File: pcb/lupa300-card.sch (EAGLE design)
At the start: 41 parts

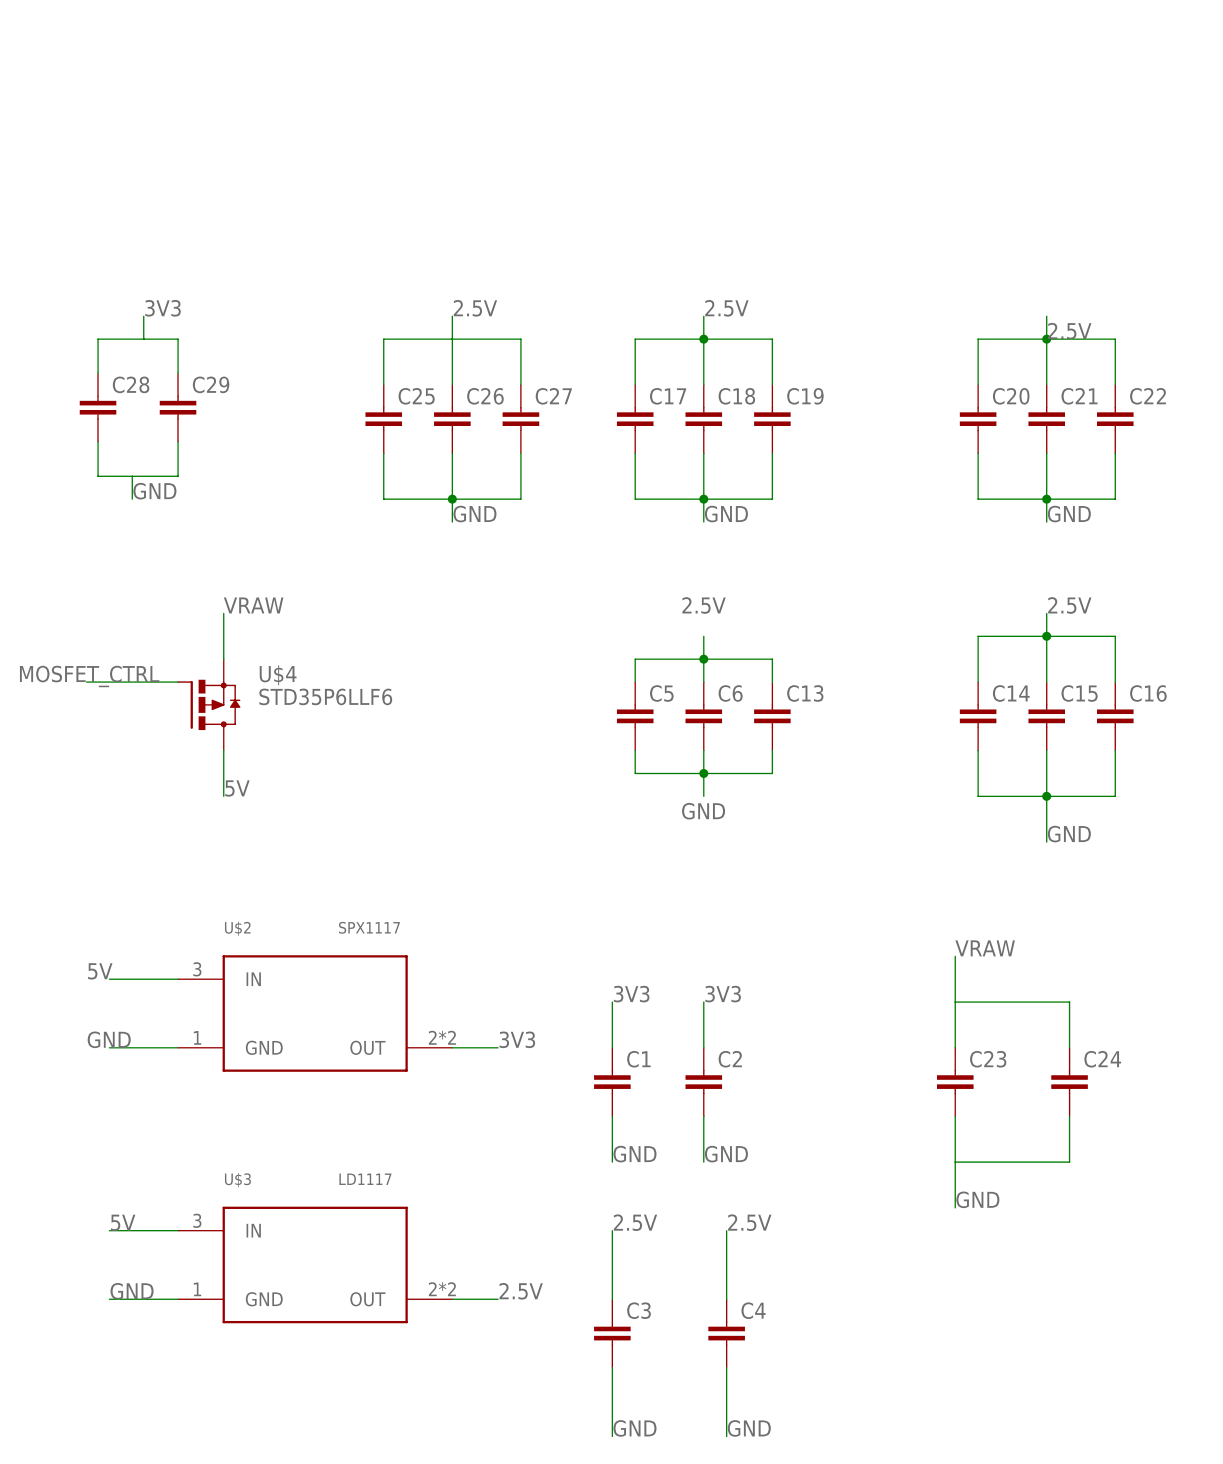
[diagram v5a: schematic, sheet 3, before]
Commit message: added all component values and added partslist
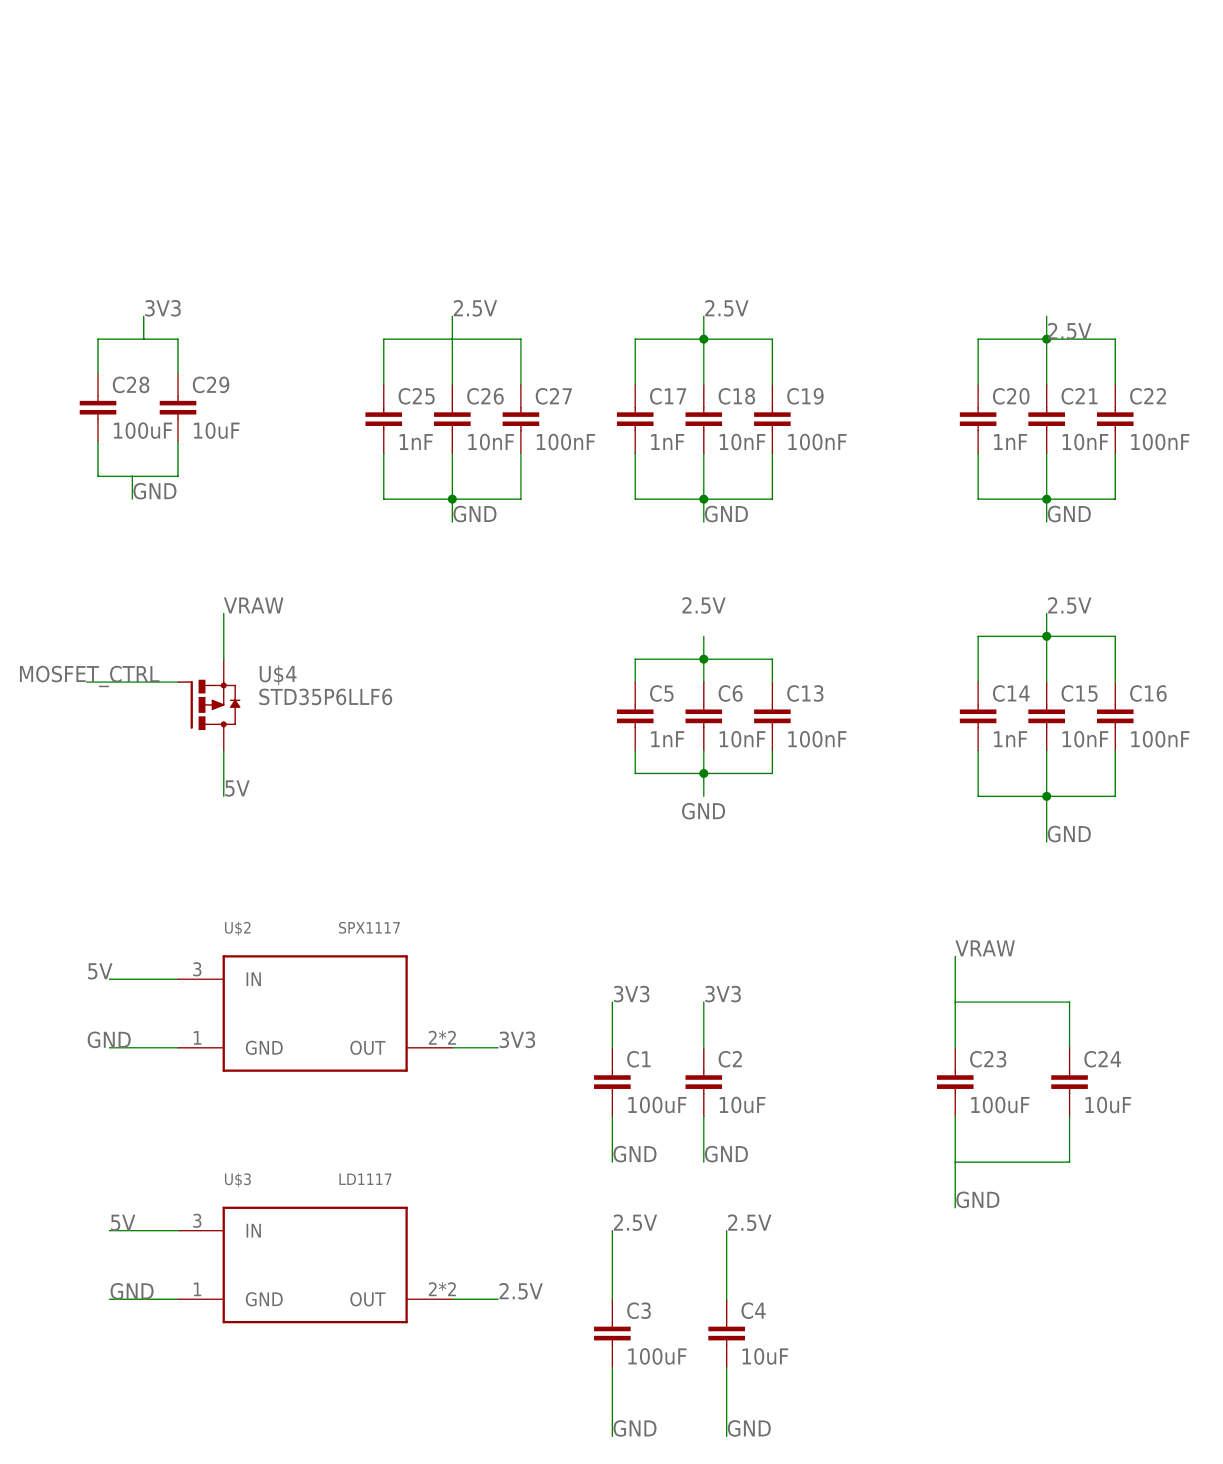
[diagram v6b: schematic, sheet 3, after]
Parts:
- C1, C23, C28, C3: value (none) -> 100uF
- C13, C16, C19, C22, C27: value (none) -> 100nF
- C14, C17, C20, C25, C5: value (none) -> 1nF
- C15, C18, C21, C26, C6: value (none) -> 10nF
- C2, C24, C29, C4: value (none) -> 10uF
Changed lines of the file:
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@@
 <?xml version="1.0" encoding="utf-8"?>
 <!DOCTYPE eagle SYSTEM "eagle.dtd">
-<eagle version="8.3.1">
+<eagle version="8.6.1">
 <drawing>
 <settings>
@@
 <part name="UZEDUPPER" library="SparkFun-Connectors" deviceset="CONN_08X2" device=""/>
 <part name="UZEDLOWER" library="SparkFun-Connectors" deviceset="CONN_08X2" device=""/>
-<part name="C1" library="rcl" library_urn="urn:adsk.eagle:library:334" deviceset="C-EU" device="C1206K" package3d_urn="urn:adsk.eagle:package:23682/2"/>
-<part name="C2" library="rcl" library_urn="urn:adsk.eagle:library:334" deviceset="C-EU" device="C1206K" package3d_urn="urn:adsk.eagle:package:23682/2"/>
-<part name="C3" library="rcl" library_urn="urn:adsk.eagle:library:334" deviceset="C-EU" device="C1206K" package3d_urn="urn:adsk.eagle:package:23682/2"/>
-<part name="C4" library="rcl" library_urn="urn:adsk.eagle:library:334" deviceset="C-EU" device="C1206K" package3d_urn="urn:adsk.eagle:package:23682/2"/>
-<part name="C5" library="rcl" library_urn="urn:adsk.eagle:library:334" deviceset="C-EU" device="C0603" package3d_urn="urn:adsk.eagle:package:23616/2"/>
-<part name="C6" library="rcl" library_urn="urn:adsk.eagle:library:334" deviceset="C-EU" device="C0603" package3d_urn="urn:adsk.eagle:package:23616/2"/>
-<part name="C13" library="rcl" library_urn="urn:adsk.eagle:library:334" deviceset="C-EU" device="C0603" package3d_urn="urn:adsk.eagle:package:23616/2"/>
-<part name="C14" library="rcl" library_urn="urn:adsk.eagle:library:334" deviceset="C-EU" device="C0603" package3d_urn="urn:adsk.eagle:package:23616/2"/>
-<part name="C15" library="rcl" library_urn="urn:adsk.eagle:library:334" deviceset="C-EU" device="C0603" package3d_urn="urn:adsk.eagle:package:23616/2"/>
-<part name="C16" library="rcl" library_urn="urn:adsk.eagle:library:334" deviceset="C-EU" device="C0603" package3d_urn="urn:adsk.eagle:package:23616/2"/>
-<part name="C17" library="rcl" library_urn="urn:adsk.eagle:library:334" deviceset="C-EU" device="C0603" package3d_urn="urn:adsk.eagle:package:23616/2"/>
-<part name="C18" library="rcl" library_urn="urn:adsk.eagle:library:334" deviceset="C-EU" device="C0603" package3d_urn="urn:adsk.eagle:package:23616/2"/>
-<part name="C19" library="rcl" library_urn="urn:adsk.eagle:library:334" deviceset="C-EU" device="C0603" package3d_urn="urn:adsk.eagle:package:23616/2"/>
-<part name="C20" library="rcl" library_urn="urn:adsk.eagle:library:334" deviceset="C-EU" device="C0603" package3d_urn="urn:adsk.eagle:package:23616/2"/>
-<part name="C21" library="rcl" library_urn="urn:adsk.eagle:library:334" deviceset="C-EU" device="C0603" package3d_urn="urn:adsk.eagle:package:23616/2"/>
-<part name="C22" library="rcl" library_urn="urn:adsk.eagle:library:334" deviceset="C-EU" device="C0603" package3d_urn="urn:adsk.eagle:package:23616/2"/>
-<part name="C23" library="rcl" library_urn="urn:adsk.eagle:library:334" deviceset="C-EU" device="C1206" package3d_urn="urn:adsk.eagle:package:23618/2"/>
-<part name="C24" library="rcl" library_urn="urn:adsk.eagle:library:334" deviceset="C-EU" device="C1206" package3d_urn="urn:adsk.eagle:package:23618/2"/>
-<part name="C25" library="rcl" library_urn="urn:adsk.eagle:library:334" deviceset="C-EU" device="C0603" package3d_urn="urn:adsk.eagle:package:23616/2"/>
-<part name="C26" library="rcl" library_urn="urn:adsk.eagle:library:334" deviceset="C-EU" device="C0603" package3d_urn="urn:adsk.eagle:package:23616/2"/>
-<part name="C27" library="rcl" library_urn="urn:adsk.eagle:library:334" deviceset="C-EU" device="C0603" package3d_urn="urn:adsk.eagle:package:23616/2"/>
-<part name="C28" library="rcl" library_urn="urn:adsk.eagle:library:334" deviceset="C-EU" device="C0603" package3d_urn="urn:adsk.eagle:package:23616/2"/>
-<part name="C29" library="rcl" library_urn="urn:adsk.eagle:library:334" deviceset="C-EU" device="C0603" package3d_urn="urn:adsk.eagle:package:23616/2"/>
+<part name="C1" library="rcl" library_urn="urn:adsk.eagle:library:334" deviceset="C-EU" device="C1206K" package3d_urn="urn:adsk.eagle:package:23682/2" value="100uF"/>
+<part name="C2" library="rcl" library_urn="urn:adsk.eagle:library:334" deviceset="C-EU" device="C1206K" package3d_urn="urn:adsk.eagle:package:23682/2" value="10uF"/>
+<part name="C3" library="rcl" library_urn="urn:adsk.eagle:library:334" deviceset="C-EU" device="C1206K" package3d_urn="urn:adsk.eagle:package:23682/2" value="100uF"/>
+<part name="C4" library="rcl" library_urn="urn:adsk.eagle:library:334" deviceset="C-EU" device="C1206K" package3d_urn="urn:adsk.eagle:package:23682/2" value="10uF"/>
+<part name="C5" library="rcl" library_urn="urn:adsk.eagle:library:334" deviceset="C-EU" device="C0603" package3d_urn="urn:adsk.eagle:package:23616/2" value="1nF"/>
+<part name="C6" library="rcl" library_urn="urn:adsk.eagle:library:334" deviceset="C-EU" device="C0603" package3d_urn="urn:adsk.eagle:package:23616/2" value="10nF"/>
+<part name="C13" library="rcl" library_urn="urn:adsk.eagle:library:334" deviceset="C-EU" device="C0603" package3d_urn="urn:adsk.eagle:package:23616/2" value="100nF"/>
+<part name="C14" library="rcl" library_urn="urn:adsk.eagle:library:334" deviceset="C-EU" device="C0603" package3d_urn="urn:adsk.eagle:package:23616/2" value="1nF"/>
+<part name="C15" library="rcl" library_urn="urn:adsk.eagle:library:334" deviceset="C-EU" device="C0603" package3d_urn="urn:adsk.eagle:package:23616/2" value="10nF"/>
+<part name="C16" library="rcl" library_urn="urn:adsk.eagle:library:334" deviceset="C-EU" device="C0603" package3d_urn="urn:adsk.eagle:package:23616/2" value="100nF"/>
+<part name="C17" library="rcl" library_urn="urn:adsk.eagle:library:334" deviceset="C-EU" device="C0603" package3d_urn="urn:adsk.eagle:package:23616/2" value="1nF"/>
+<part name="C18" library="rcl" library_urn="urn:adsk.eagle:library:334" deviceset="C-EU" device="C0603" package3d_urn="urn:adsk.eagle:package:23616/2" value="10nF"/>
+<part name="C19" library="rcl" library_urn="urn:adsk.eagle:library:334" deviceset="C-EU" device="C0603" package3d_urn="urn:adsk.eagle:package:23616/2" value="100nF"/>
+<part name="C20" library="rcl" library_urn="urn:adsk.eagle:library:334" deviceset="C-EU" device="C0603" package3d_urn="urn:adsk.eagle:package:23616/2" value="1nF"/>
+<part name="C21" library="rcl" library_urn="urn:adsk.eagle:library:334" deviceset="C-EU" device="C0603" package3d_urn="urn:adsk.eagle:package:23616/2" value="10nF"/>
+<part name="C22" library="rcl" library_urn="urn:adsk.eagle:library:334" deviceset="C-EU" device="C0603" package3d_urn="urn:adsk.eagle:package:23616/2" value="100nF"/>
+<part name="C23" library="rcl" library_urn="urn:adsk.eagle:library:334" deviceset="C-EU" device="C1206" package3d_urn="urn:adsk.eagle:package:23618/2" value="100uF"/>
+<part name="C24" library="rcl" library_urn="urn:adsk.eagle:library:334" deviceset="C-EU" device="C1206" package3d_urn="urn:adsk.eagle:package:23618/2" value="10uF"/>
+<part name="C25" library="rcl" library_urn="urn:adsk.eagle:library:334" deviceset="C-EU" device="C0603" package3d_urn="urn:adsk.eagle:package:23616/2" value="1nF"/>
+<part name="C26" library="rcl" library_urn="urn:adsk.eagle:library:334" deviceset="C-EU" device="C0603" package3d_urn="urn:adsk.eagle:package:23616/2" value="10nF"/>
+<part name="C27" library="rcl" library_urn="urn:adsk.eagle:library:334" deviceset="C-EU" device="C0603" package3d_urn="urn:adsk.eagle:package:23616/2" value="100nF"/>
+<part name="C28" library="rcl" library_urn="urn:adsk.eagle:library:334" deviceset="C-EU" device="C0603" package3d_urn="urn:adsk.eagle:package:23616/2" value="100uF"/>
+<part name="C29" library="rcl" library_urn="urn:adsk.eagle:library:334" deviceset="C-EU" device="C0603" package3d_urn="urn:adsk.eagle:package:23616/2" value="10uF"/>
 </parts>
 <sheets>
